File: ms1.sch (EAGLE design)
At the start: 148 parts, among them IC1 MAX3232EUE, IC2 MAX3380EEUP, J1 POWERPOLE_POWER25A, J10 Radio, J11 A3, J12 A4, J13 A5, J14 A6, J15 A7, J16 D1, J17 D2, J18 D3, J19 D4, J2 ON, J20 D5, J21 D6, J22 D7, J3 LED-EN, J4 RS232, J5 RS485, J6 A1, J7 I2C, J8 A2, J9 TTL_SERIAL, Q1 DMG6602SVT, Q2 DMG6602SVT, Q3 DMG6602SVT, Q4 DMG6602SVT, U1 LT1934ES6TRMPBF, U2 LT1934ES6TRMPBF, U3 DS3231SN, U4 ISL3179EIBZ, X1 KUSBVX-BS1N

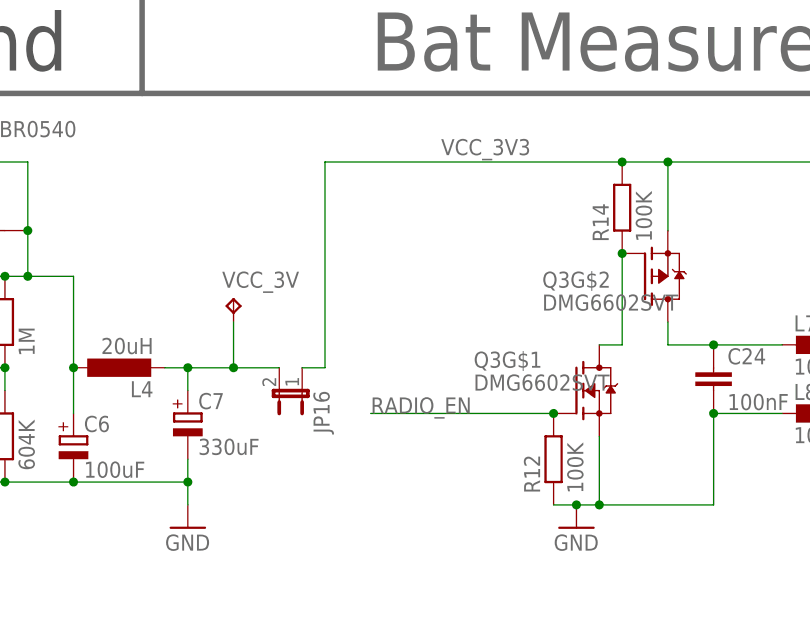
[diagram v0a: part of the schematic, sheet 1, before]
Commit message: more smoothing on 3v3 output
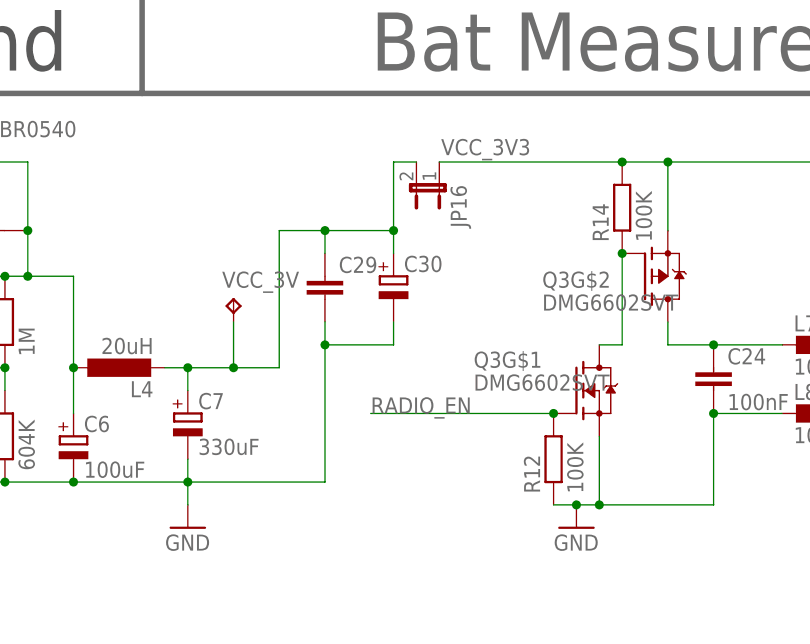
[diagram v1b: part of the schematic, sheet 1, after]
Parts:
- added C29: (no value), resistor:C-EUC0805
- added C30: (no value), resistor:CPOL-EUB/3528-21R
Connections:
- net GND: now also C29.2, C30.-
- net N$13: now also C29.1, C30.+
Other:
- moved on the sheet: JP16
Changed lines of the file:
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@@
 <part name="JP8" library="SparkFun-Passives" deviceset="JUMPER-2" device="SMD-NO"/>
 <part name="JP16" library="SparkFun-Passives" deviceset="JUMPER-2" device="SMD-NO"/>
+<part name="C29" library="resistor" deviceset="C-EU" device="C0805"/>
+<part name="C30" library="resistor" deviceset="CPOL-EU" device="B/3528-21R"/>
 </parts>
 <sheets>
@@
 <instance part="C28" gate="G$1" x="350.52" y="55.88"/>
 <instance part="JP8" gate="A" x="358.14" y="63.5"/>
-<instance part="JP16" gate="A" x="121.92" y="149.86" rot="R180"/>
+<instance part="JP16" gate="A" x="137.16" y="172.72" rot="R180"/>
+<instance part="C29" gate="G$1" x="124.46" y="162.56"/>
+<instance part="C30" gate="G$1" x="132.08" y="162.56"/>
 </instances>
 <busses>
@@
 <junction x="109.22" y="139.7"/>
 <junction x="96.52" y="139.7"/>
+<pinref part="C30" gate="G$1" pin="-"/>
+<wire x1="124.46" y1="139.7" x2="124.46" y2="154.94" width="0.1524" layer="91"/>
+<wire x1="124.46" y1="154.94" x2="132.08" y2="154.94" width="0.1524" layer="91"/>
+<wire x1="132.08" y1="154.94" x2="132.08" y2="157.48" width="0.1524" layer="91"/>
+<pinref part="C29" gate="G$1" pin="2"/>
+<wire x1="124.46" y1="157.48" x2="124.46" y2="154.94" width="0.1524" layer="91"/>
+<junction x="124.46" y="154.94"/>
+<wire x1="124.46" y1="139.7" x2="109.22" y2="139.7" width="0.1524" layer="91"/>
 </segment>
 <segment>
@@
 <pinref part="R14" gate="G$1" pin="2"/>
 <label x="147.32" y="177.8" size="1.778" layer="95" rot="R180"/>
-<wire x1="157.48" y1="175.26" x2="124.46" y2="175.26" width="0.1524" layer="91"/>
-<wire x1="124.46" y1="175.26" x2="124.46" y2="152.4" width="0.1524" layer="91"/>
+<wire x1="157.48" y1="175.26" x2="137.16" y2="175.26" width="0.1524" layer="91"/>
 <pinref part="Q4" gate="G$2" pin="S"/>
 <wire x1="322.58" y1="167.64" x2="322.58" y2="175.26" width="0.1524" layer="91"/>
@@
 <junction x="317.5" y="175.26"/>
 <pinref part="JP16" gate="A" pin="1"/>
-<wire x1="121.92" y1="152.4" x2="124.46" y2="152.4" width="0.1524" layer="91"/>
 </segment>
 <segment>
@@
 <wire x1="114.3" y1="152.4" x2="114.3" y2="157.48" width="0.1524" layer="91"/>
 <junction x="109.22" y="152.4"/>
+<wire x1="114.3" y1="152.4" x2="119.38" y2="152.4" width="0.1524" layer="91"/>
+<wire x1="119.38" y1="152.4" x2="119.38" y2="167.64" width="0.1524" layer="91"/>
+<wire x1="119.38" y1="167.64" x2="124.46" y2="167.64" width="0.1524" layer="91"/>
+<wire x1="124.46" y1="167.64" x2="132.08" y2="167.64" width="0.1524" layer="91"/>
+<pinref part="C29" gate="G$1" pin="1"/>
+<wire x1="124.46" y1="167.64" x2="124.46" y2="165.1" width="0.1524" layer="91"/>
+<pinref part="C30" gate="G$1" pin="+"/>
+<wire x1="132.08" y1="165.1" x2="132.08" y2="167.64" width="0.1524" layer="91"/>
+<junction x="124.46" y="167.64"/>
+<junction x="114.3" y="152.4"/>
 <pinref part="JP16" gate="A" pin="2"/>
-<wire x1="119.38" y1="152.4" x2="114.3" y2="152.4" width="0.1524" layer="91"/>
-<junction x="114.3" y="152.4"/>
-</segment>
-</net>
+<wire x1="134.62" y1="175.26" x2="132.08" y2="175.26" width="0.1524" layer="91"/>
+<wire x1="132.08" y1="175.26" x2="132.08" y2="167.64" width="0.1524" layer="91"/>
+<junction x="132.08" y="167.64"/>
+</segment>
+</net>

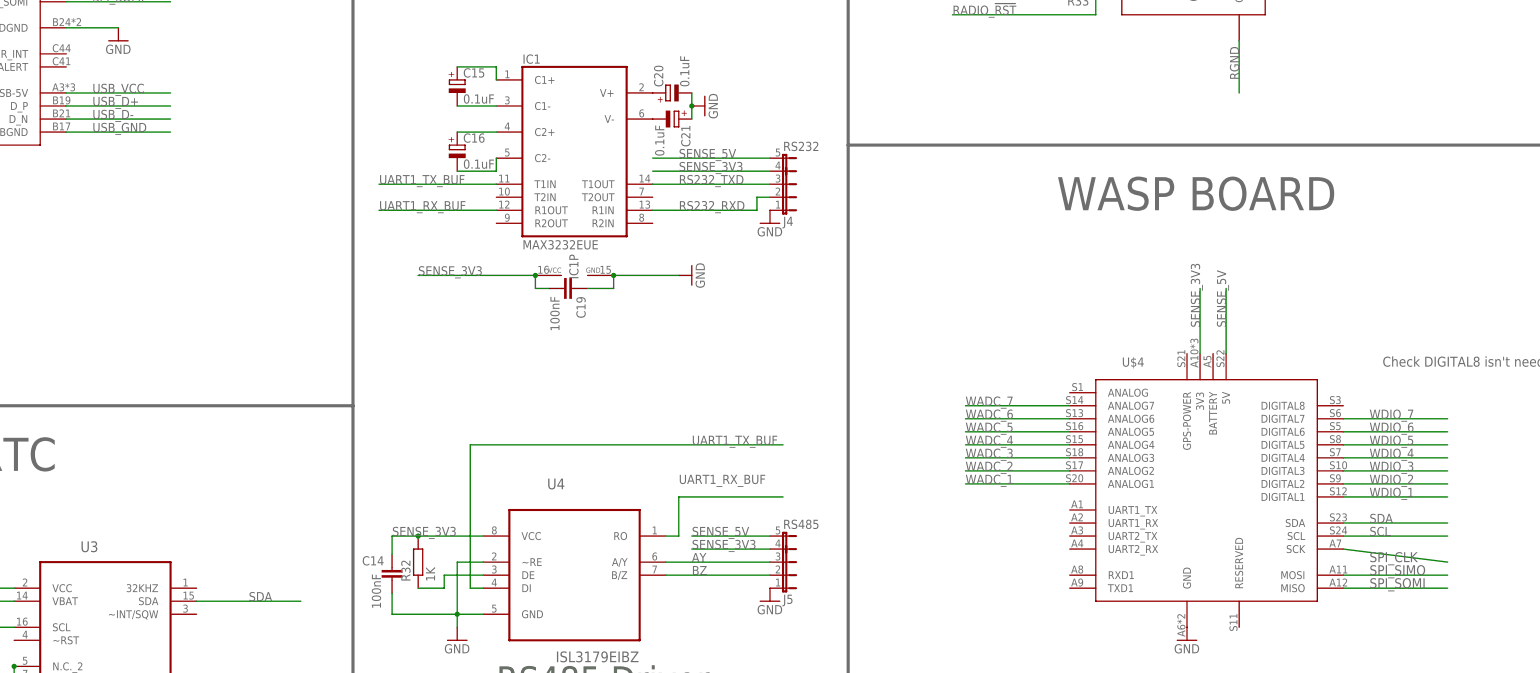
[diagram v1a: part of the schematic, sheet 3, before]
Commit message: more routing - mainly digital signals
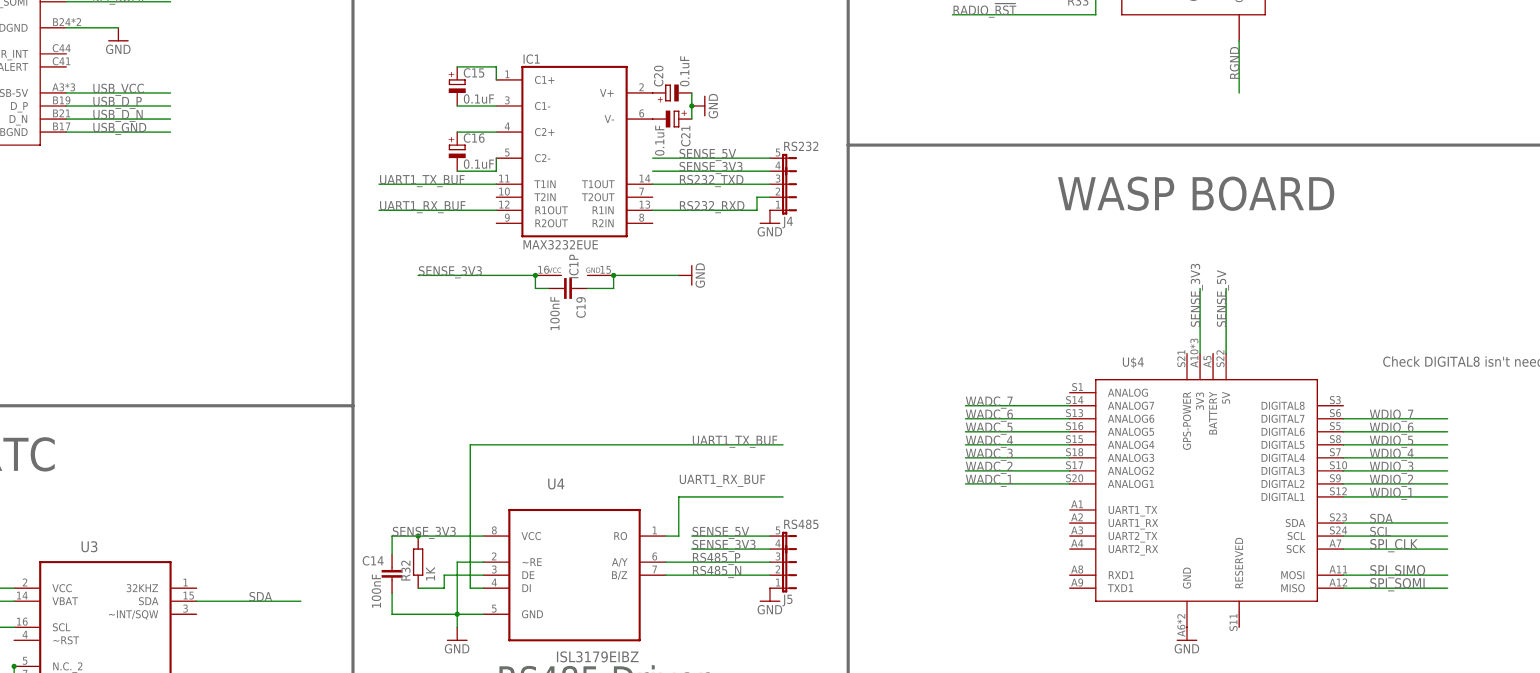
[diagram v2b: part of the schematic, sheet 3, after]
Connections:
- net AY renamed RS485_P
- net BZ renamed RS485_N
- net USB_D+ renamed USB_D_P
- net USB_D- renamed USB_D_N
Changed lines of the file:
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@@
 <?xml version="1.0" encoding="utf-8"?>
 <!DOCTYPE eagle SYSTEM "eagle.dtd">
-<eagle version="6.5.0">
+<eagle version="6.6.0">
 <drawing>
 <settings>
@@
 <classes>
 <class number="0" name="default" width="0" drill="0">
+</class>
+<class number="1" name="usb" width="0.3048" drill="0.3556">
+<clearance class="1" value="0.1524"/>
+</class>
+<class number="2" name="rs485" width="0.3048" drill="0.3556">
+<clearance class="2" value="0.3048"/>
 </class>
 </classes>
@@
 </segment>
 </net>
-<net name="USB_D-" class="0">
+<net name="USB_D_N" class="0">
 <segment>
 <pinref part="X1" gate="G$1" pin="2"/>
@@
 </segment>
 </net>
-<net name="USB_D+" class="0">
+<net name="USB_D_P" class="0">
 <segment>
 <pinref part="X1" gate="G$1" pin="3"/>
@@
 <segment>
 <pinref part="U$4" gate="G$1" pin="SCK"/>
-<wire x1="337.82" y1="76.2" x2="358.14" y2="73.66" width="0.1524" layer="91"/>
-<label x="342.9" y="73.66" size="1.9304" layer="95"/>
+<wire x1="337.82" y1="76.2" x2="358.14" y2="76.2" width="0.1524" layer="91"/>
+<label x="342.9" y="76.2" size="1.9304" layer="95"/>
 </segment>
 <segment>
@@
 </segment>
 </net>
-<net name="USB_D+" class="0">
+<net name="USB_D_P" class="0">
 <segment>
 <pinref part="U$2" gate="G$1" pin="D_P"/>
@@
 </segment>
 </net>
-<net name="USB_D-" class="0">
+<net name="USB_D_N" class="0">
 <segment>
 <pinref part="U$2" gate="G$1" pin="D_N"/>
@@
 </segment>
 </net>
-<net name="BZ" class="0">
+<net name="RS485_N" class="2">
 <segment>
 <wire x1="205.74" y1="71.12" x2="226.06" y2="71.12" width="0.1524" layer="91"/>
@@
 </segment>
 </net>
-<net name="AY" class="0">
+<net name="RS485_P" class="2">
 <segment>
 <pinref part="U4" gate="A" pin="A/Y"/>
